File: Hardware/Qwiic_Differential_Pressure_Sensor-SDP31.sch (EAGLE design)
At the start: 27 parts, among them J2 QWIIC_RIGHT_ANGLE, J4 QWIIC_RIGHT_ANGLE, U1 SDP31

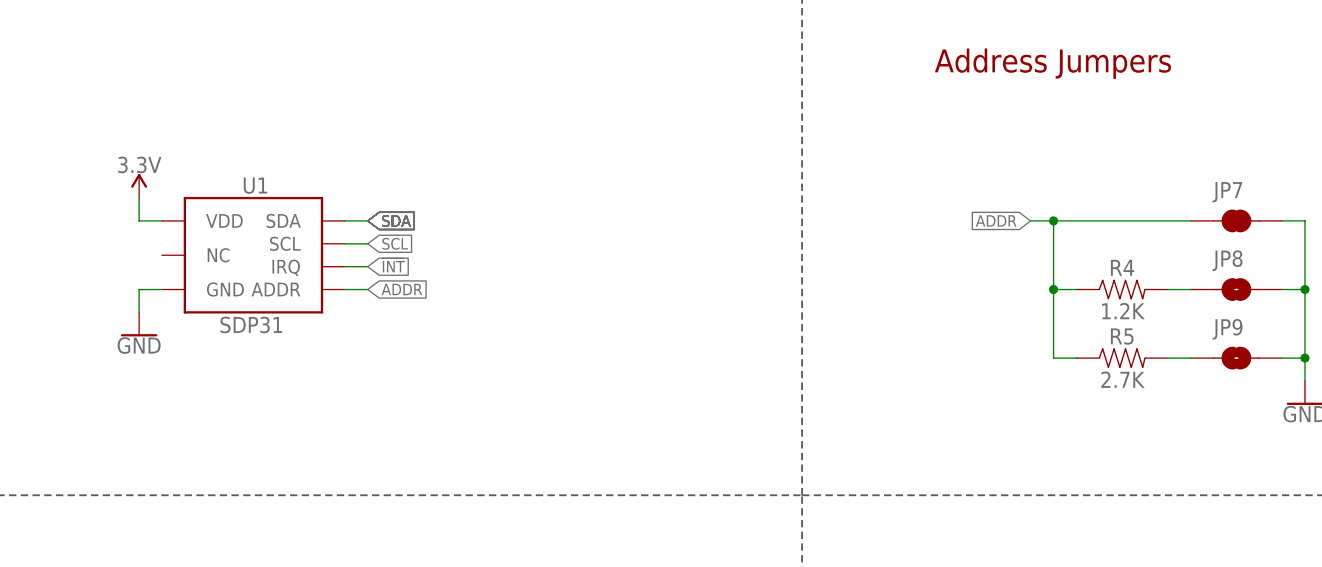
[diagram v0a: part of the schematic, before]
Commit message: Update PROD_IDs. Delete New-Parts
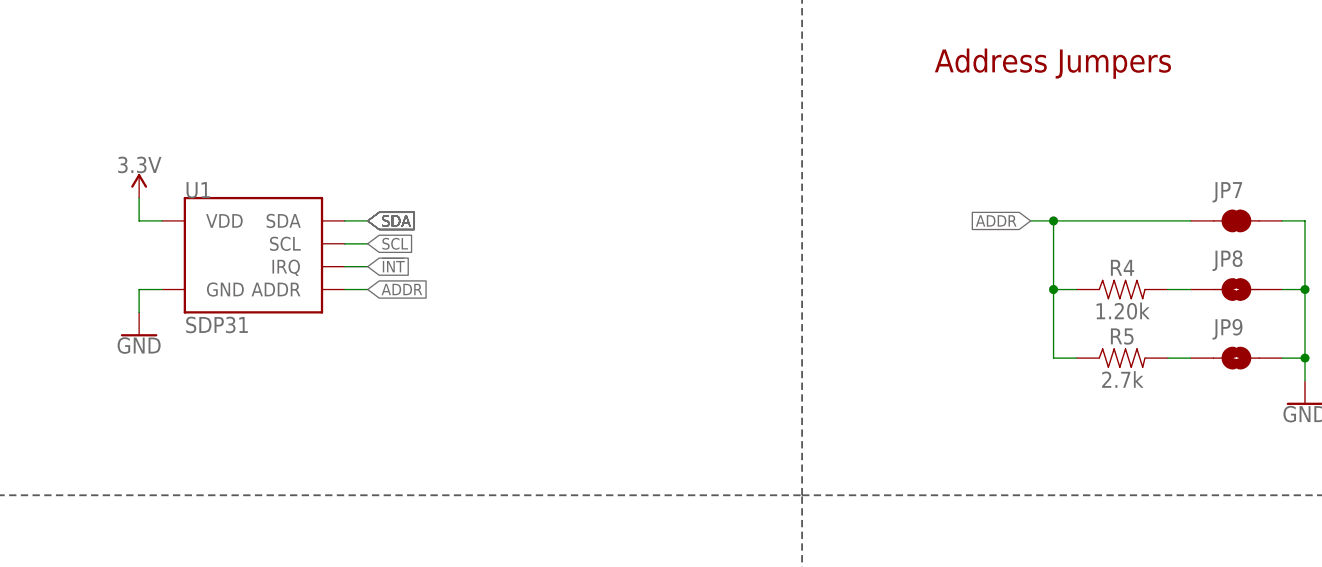
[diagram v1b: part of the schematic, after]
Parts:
- JP1, JP2, JP5, JP6: device SparkFun:FIDUCIALUFIDUCIAL -> SparkFun-Aesthetics:FIDUCIALUFIDUCIAL
- JP3, JP4: device SparkFun:STAND-OFF -> SparkFun-Hardware:STAND-OFF
- R4: value 1.2K -> 1.20k; device New-Parts_SparkFun-Resistors:1.2K-0603-1/10W-1% -> SparkFun-Resistors:1.20KOHM-0603-1/10W-1%
- R5: value 2.7K -> 2.7k; device New-Parts_SparkFun-Resistors:2.7K-0603-1/10W-1% -> SparkFun-Resistors:2.7KOHM-0603-1/10W-1%
- U1: device New-Parts_SparkFun-Sensors:SDP31 -> SparkFun-Sensors:SDP3X_SDP31
